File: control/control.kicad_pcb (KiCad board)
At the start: 2 copper layers, 23 x 84 mm, 4 parts, among them J1 CONTROL

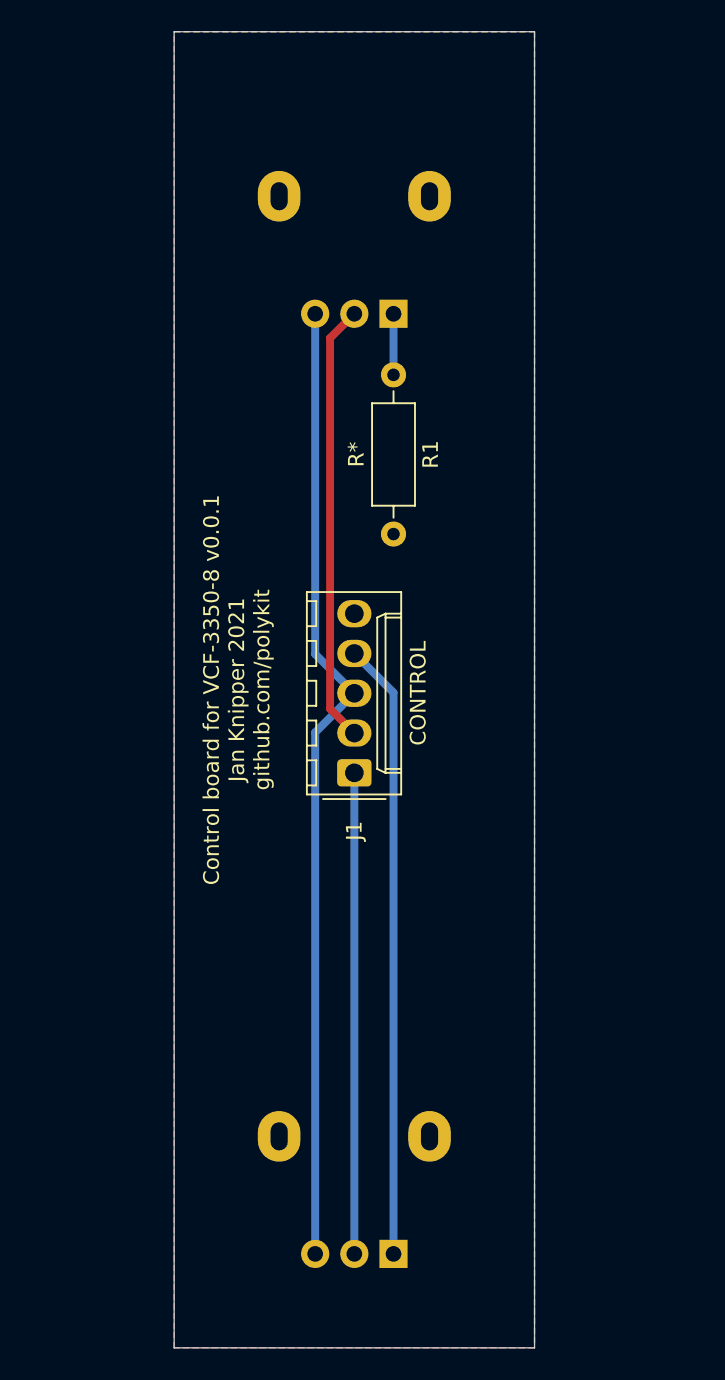
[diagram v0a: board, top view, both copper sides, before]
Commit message: Update control board
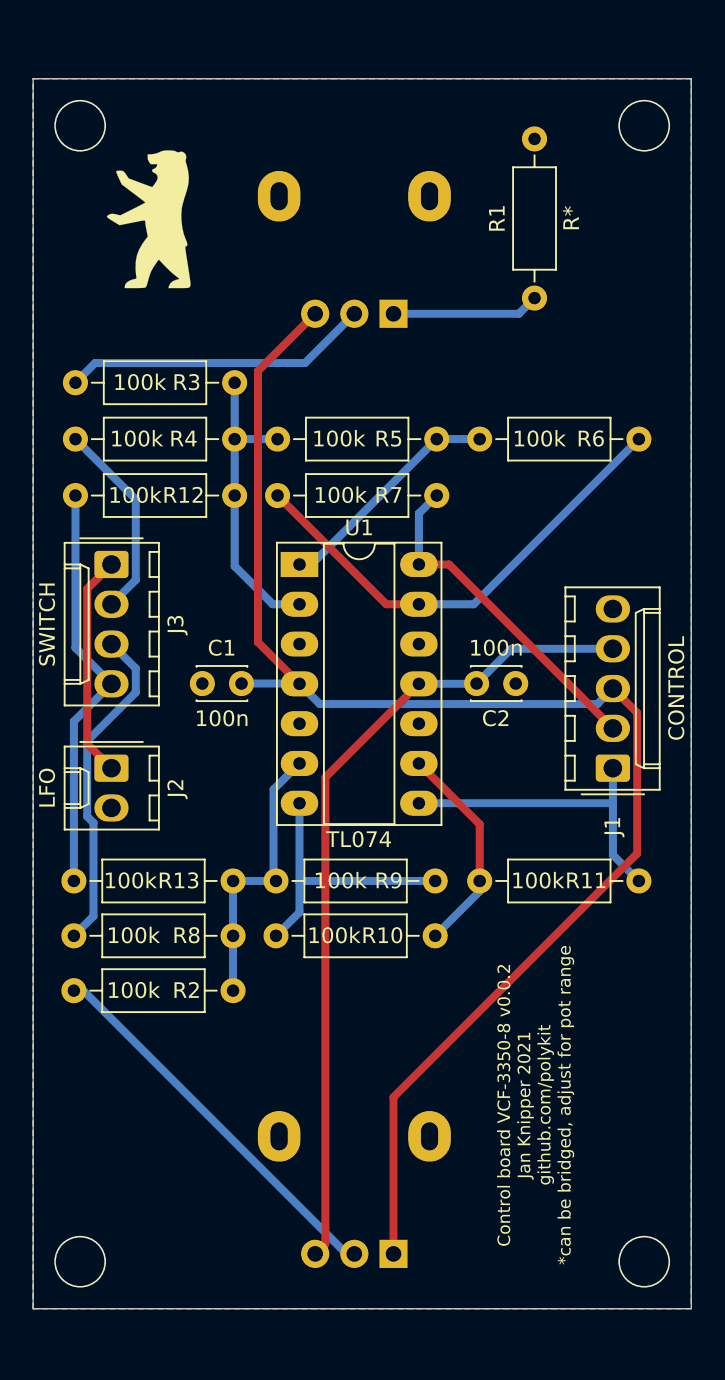
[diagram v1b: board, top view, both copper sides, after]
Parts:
- added C1: 100n, Capacitor_THT:C_Disc_D3.0mm_W2.0mm_P2.50mm, F.Cu at (76.8, 93.6)
- added C2: 100n, Capacitor_THT:C_Disc_D3.0mm_W2.0mm_P2.50mm, F.Cu at (96.8, 93.6)
- added G***: LOGO, Polykit:bär-small, F.Cu at (73.5, 64.0)
- added J2: LFO, Connector_Molex:Molex_KK-254_AE-6410-02A_1x02_P2.54mm_Vertical, F.Cu at (71.0, 99.0)
- added J3: SWITCH, Connector_Molex:Molex_KK-254_AE-6410-04A_1x04_P2.54mm_Vertical, F.Cu at (71.0, 86.0)
- added R10: 100k, Resistor_THT:R_Axial_DIN0207_L6.3mm_D2.5mm_P10.16mm_Horizontal, F.Cu at (81.5, 109.7)
- added R11: 100k, Resistor_THT:R_Axial_DIN0207_L6.3mm_D2.5mm_P10.16mm_Horizontal, F.Cu at (94.5, 106.2)
- added R12: 100k, Resistor_THT:R_Axial_DIN0207_L6.3mm_D2.5mm_P10.16mm_Horizontal, F.Cu at (68.7, 81.6)
- added R13: 100k, Resistor_THT:R_Axial_DIN0207_L6.3mm_D2.5mm_P10.16mm_Horizontal, F.Cu at (68.6, 106.2)
- added R2: 100k, Resistor_THT:R_Axial_DIN0207_L6.3mm_D2.5mm_P10.16mm_Horizontal, F.Cu at (68.6, 113.2)
- added R3: 100k, Resistor_THT:R_Axial_DIN0207_L6.3mm_D2.5mm_P10.16mm_Horizontal, F.Cu at (68.7, 74.4)
- added R4: 100k, Resistor_THT:R_Axial_DIN0207_L6.3mm_D2.5mm_P10.16mm_Horizontal, F.Cu at (68.7, 78.0)
- added R5: 100k, Resistor_THT:R_Axial_DIN0207_L6.3mm_D2.5mm_P10.16mm_Horizontal, F.Cu at (81.6, 78.0)
- added R6: 100k, Resistor_THT:R_Axial_DIN0207_L6.3mm_D2.5mm_P10.16mm_Horizontal, F.Cu at (94.5, 78.0)
- added R7: 100k, Resistor_THT:R_Axial_DIN0207_L6.3mm_D2.5mm_P10.16mm_Horizontal, F.Cu at (81.6, 81.6)
- added R8: 100k, Resistor_THT:R_Axial_DIN0207_L6.3mm_D2.5mm_P10.16mm_Horizontal, F.Cu at (68.6, 109.7)
- added R9: 100k, Resistor_THT:R_Axial_DIN0207_L6.3mm_D2.5mm_P10.16mm_Horizontal, F.Cu at (81.5, 106.2)
- added U1: TL074, Package_DIP:DIP-14_W7.62mm_Socket_LongPads, F.Cu at (83.0, 86.0)
- RV1: value FREQ -> FREQ 100k
- RV2: value RES -> RES 100k
- moved J1 16.5 mm to (103.0, 99.0)
- moved R1 10.2 mm to (98.0, 69.0), turned to 90 degrees
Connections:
- RV1 pad 2: FREQ -> POT_FREQ
- RV2 pad 1: -12V -> +12V
- RV2 pad 2: RES -> POT_RES
- RV2 pad 3: +12V -> -12V
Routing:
- net +12V: track 62.1 -> 94.0 mm
- net Net-(R6-Pad2): track 0.00 -> 30.3 mm
- net SW_FREQ_RES: track 0.00 -> 26.5 mm
- net POT_RES: track 0.00 -> 24.9 mm
- net SW_RES: track 0.00 -> 21.2 mm
- net POT_FREQ: track 0.00 -> 19.6 mm
- net Net-(R12-Pad2): track 0.00 -> 19.6 mm
- net Net-(R13-Pad2): track 0.00 -> 18.0 mm
- net Net-(R10-Pad1): track 0.00 -> 17.8 mm
- net Net-(R5-Pad2): track 0.00 -> 14.8 mm
- net LFO: track 0.00 -> 14.3 mm
- net Net-(R10-Pad2): track 0.00 -> 13.8 mm
- net -12V: track 39.4 -> 52.4 mm
- net SW_FREQ: track 0.00 -> 12.8 mm
- net RES: track 30.7 -> 20.3 mm
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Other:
- board size 23 x 84 mm -> 42 x 78.5 mm
- board text added: "Control board VCF-3350-8 v0.0.2 Jan Knipper 2021 github.com/polykit *can be bridged, adjust for pot range"
- board text removed: "Control board for VCF-3350-8 v0.0.1 Jan Knipper 2021 github.com/polykit"
